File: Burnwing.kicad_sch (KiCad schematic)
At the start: 55 parts, among them J1 Conn_01x03_Pin, J2 USB Type C, J3 Conn_01x02_Pin, J5 Conn_01x06_MountingPin, J6 Conn_01x06_MountingPin, Q1 AONR21307, SW1 SW_DIP_x02, U1 HUSB238, U2 BTS7030-2EPA, U3 TPS70933QDBVRQ1

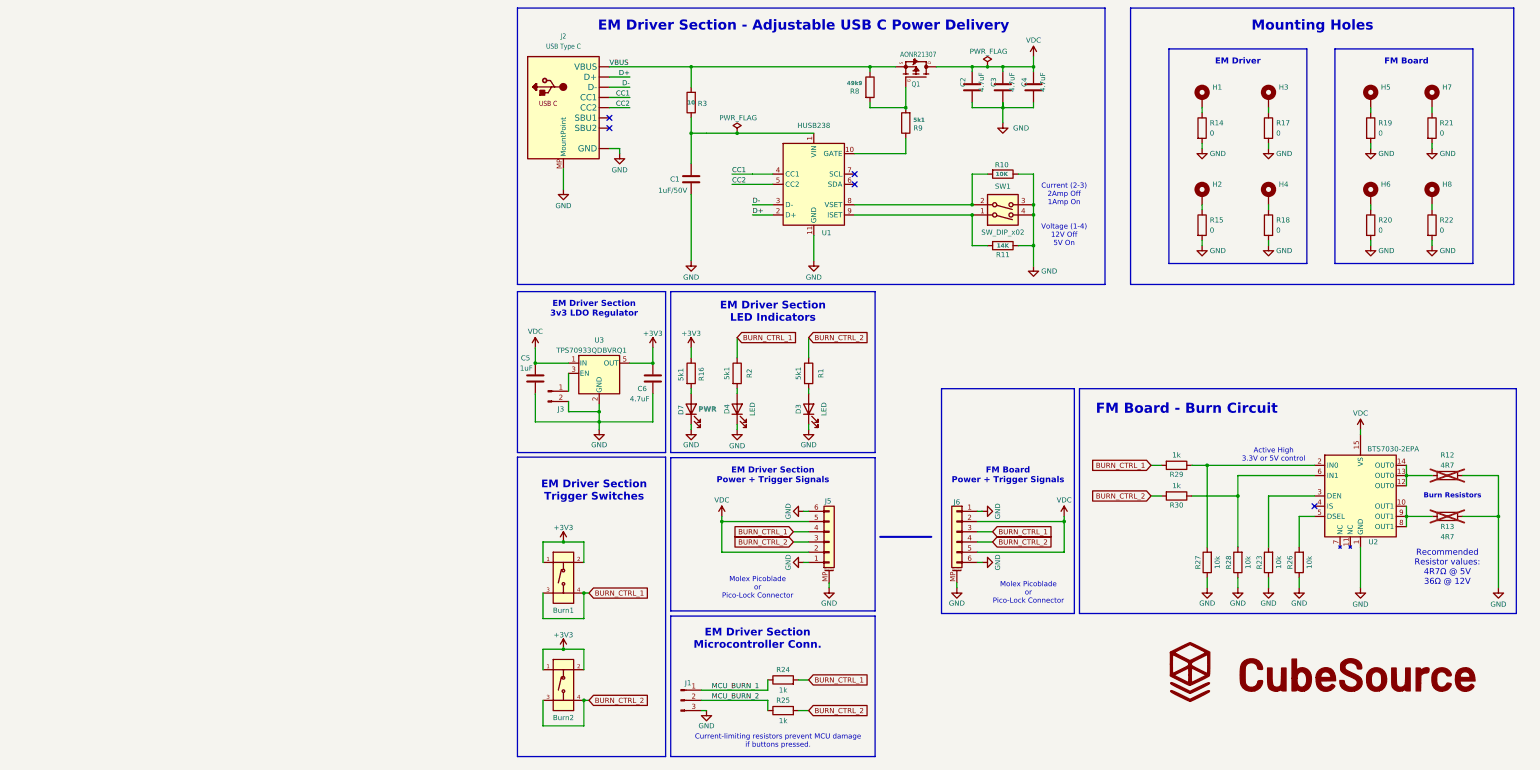
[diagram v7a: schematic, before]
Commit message: Cleaned up layout and libraries
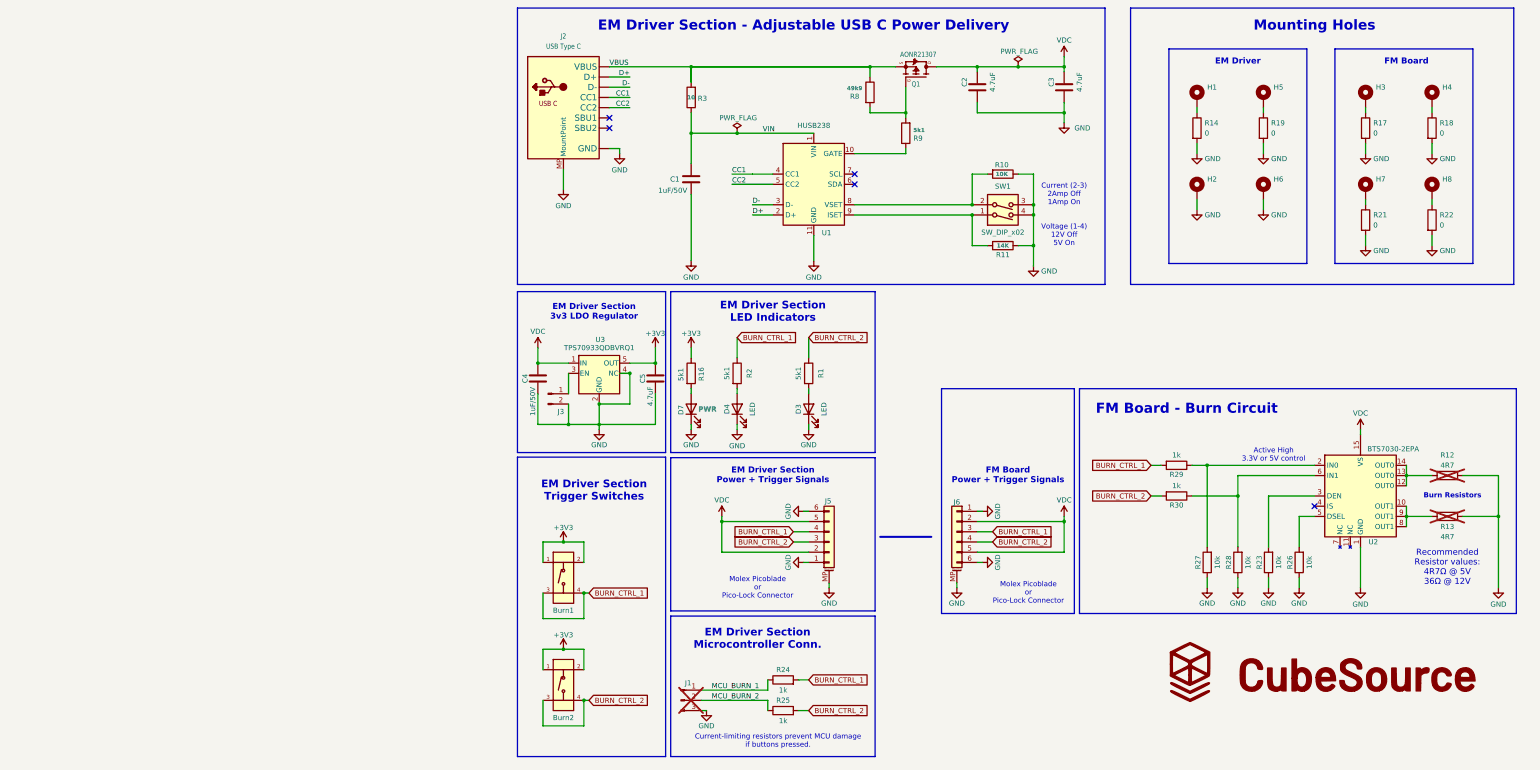
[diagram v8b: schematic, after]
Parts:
- removed C6: 4.7uF, Capacitor_SMD:C_0805_2012Metric_Pad1.18x1.45mm_HandSolder, symbol Device:C
- removed R15, R20: 0, Resistor_SMD:R_0603_1608Metric_Pad0.98x0.95mm_HandSolder, symbol Device:R
- Burn1, Burn2: footprint 00-Project-Footprint-Lib:KEY-SMD_4P-L6.0-W6.0-P4.50-LS9.5-BR -> Burnwing:KEY-SMD_4P-L6.0-W6.0-P4.50-LS9.5-BR; symbol 00-Project-Symbol-Lib:Tactile_Button -> Burnwing:Tactile_Button
- C4: value 4.7uF -> 1uF/50V; LCSC C437557 -> C28323
- C5: value 1uF -> 4.7uF; LCSC (none) -> C437557
- J1: now not fitted; now left out of the parts list
- J2: footprint 00-Project-Footprint-Lib:USB_C_CUSB31-CFM2AX-01-X -> Burnwing:USB_C_CUSB31-CFM2AX-01-X; symbol 00-Project-Symbol-Lib:USB_C_CUSB31-CFM2AX-01-X -> Burnwing:USB_C_CUSB31-CFM2AX-01-X
- J5: value Conn_01x06_MountingPin -> Conn_01x06_MountingPin-Mirror; footprint 00-Project-Footprint-Lib:Molex_Pico-Lock_and_PicoBlade -> Burnwing:Molex_Pico-Lock_and_PicoBlade
- J6: footprint 00-Project-Footprint-Lib:Molex_Pico-Lock_and_PicoBlade -> Burnwing:Molex_Pico-Lock_and_PicoBlade
- Q1: footprint 00-Project-Footprint-Lib:POWERDI3333 -> Burnwing:POWERDI3333; symbol 00-Project-Symbol-Lib:AONR21307_PMOSFET -> Burnwing:AONR21307_PMOSFET
- R12, R13: footprint 00-Project-Footprint-Lib:AxialBurnResistor_No_Cutout -> Burnwing:AxialBurnResistor_No_Cutout
- SW1: footprint 00-Project-Footprint-Lib:2_Dipswitch -> Burnwing:2_Dipswitch
- U2: footprint 00-Project-Footprint-Lib:PG-TSDSO-14_L4.9-W3.9-P0.65-LS6.0-BL-EP -> Burnwing:PG-TSDSO-14_L4.9-W3.9-P0.65-LS6.0-BL-EP; symbol 00-Project-Symbol-Lib:BTS7030-2EPA -> Burnwing:BTS7030-2EPA
- U3: footprint Package_TO_SOT_SMD:SOT-23-5 -> Burnwing:SOT-23-5; symbol 00-Project-Symbol-Lib:TPS70933QDBVRQ1 -> Burnwing:TPS70933QDBVRQ1
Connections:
- net +3V3: now also C5.1
- net GND: now also H2.1, H6.1, U3.4 (NC)
- net VDC: no longer C5.1
- net VIN: now reaches C1.1, R3.1, U1.1 (VIN)
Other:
- moved on the sheet: C2, C3, H1, H2, H3, H4, H5, H6, H7, H8, J3, R14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
